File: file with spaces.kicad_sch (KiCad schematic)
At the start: 0 parts

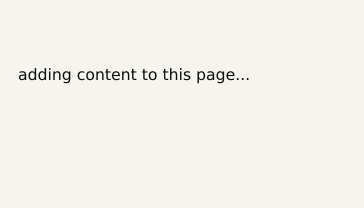
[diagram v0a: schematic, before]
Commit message: Add content to the new page. It cannot be labels.
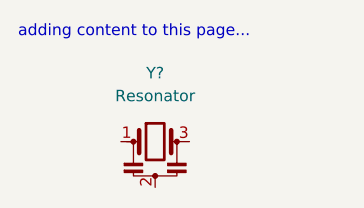
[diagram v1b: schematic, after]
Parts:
- added Y?: Resonator, symbol Device:Resonator
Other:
- note added: "adding content to this page..."
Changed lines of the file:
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@@
 (kicad_sch (version 20211123) (generator eeschema)
   (paper "A4")
-  (label "adding content to this page..." (at 137.16 102.87 0)
+  (text "adding content to this page..." (at 137.16 97.79 0)
     (effects (font (size 1.27 1.27)) (justify left bottom))
   )
+  (symbol (lib_id "Device:Resonator") (at 152.4 109.22 0) (unit 1)
+    (in_bom yes) (on_board yes) (fields_autoplaced)
+    (property "Reference" "Y?" (id 0) (at 152.4 101.6 0))
+    (property "Value" "Resonator" (id 1) (at 152.4 104.14 0))
+    (property "Footprint" "" (id 2) (at 151.765 109.22 0)
+      (effects (font (size 1.27 1.27)) hide)
+    )
+    (property "Datasheet" "~" (id 3) (at 151.765 109.22 0)
+      (effects (font (size 1.27 1.27)) hide)
+    )
+    (pin "1")
+    (pin "2")
+    (pin "3")
+  )
 )
